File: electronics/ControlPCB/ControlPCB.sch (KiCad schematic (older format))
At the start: 29 parts, among them CON1 BARREL_JACK, P1 Opto1, P2 Opto2, P3 Opto3, P4 Opto4, P5 Opto5, P6 Opto6, P7 Tool, U1 POLOLU_A4988, U2 POLOLU_A4988, U3 POLOLU_A4988, U4 POLOLU_A4988, U5 POLOLU_A4988, U6 POLOLU_A4988, U7 POLOLU_A4988

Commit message: ControlPCB Kicad project update
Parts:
- added PA1: AUX12V, Pin_Headers:Pin_Header_Straight_2x03, symbol CONN_02X03
- added PA2: AUX5V, Pin_Headers:Pin_Header_Straight_2x03, symbol CONN_02X03
- added PDIG1: CONN_02X18, Pin_Headers:Pin_Header_Straight_2x18, symbol CONN_02X18
- added PI1: VCCINPUT, Pin_Headers:Pin_Header_Straight_1x02, symbol CONN_01X02
- added PM1, PM2, PM3, PM4, PM5, PM6, PM7: CONN_01X04, Pin_Headers:Pin_Header_Straight_1x04, symbol CONN_01X04
- C1, C2, C3, C4, C5, C6, C7: footprint (none) -> Capacitors_ThroughHole:C_Radial_D6.3_L11.2_P2.5
- CON1: value BARREL_JACK -> 12VINPUT; footprint (none) -> Connect:BARREL_JACK
- P1, P2, P3, P4, P5, P6, P7: footprint (none) -> Pin_Headers:Pin_Header_Straight_1x03
- R1, R2, R3, R4, R5, R6, R7: footprint (none) -> Resistors_ThroughHole:Resistor_Horizontal_RM7mm
- U1, U2, U3, U4, U5, U6, U7: footprint (none) -> POL:POLA4988
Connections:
- net +12V: now also PA1.2 (P2), PA1.4 (P4), PA1.6 (P6)
- net 1AM1: now also PM1.3 (P3)
- net 1AM2: now also PM2.3 (P3)
- net 1AM3: now also PM3.3 (P3)
- net 1AM4: now also PM4.3 (P3)
- net 1AM5: now also PM5.3 (P3)
- net 1AM6: now also PM6.3 (P3)
- net 1AM7: now also PM7.3 (P3)
- net 1BM1: now also PM1.4 (P4)
- net 1BM2: now also PM2.4 (P4)
- net 1BM3: now also PM3.4 (P4)
- net 1BM4: now also PM4.4 (P4)
- net 1BM5: now also PM5.4 (P4)
- net 1BM6: now also PM6.4 (P4)
- net 1BM7: now also PM7.4 (P4)
- net 2AM1: now also PM1.2 (P2)
- net 2AM2: now also PM2.2 (P2)
- net 2AM3: now also PM3.2 (P2)
- net 2AM4: now also PM4.2 (P2)
- net 2AM5: now also PM5.2 (P2)
- net 2AM6: now also PM6.2 (P2)
- net 2AM7: now also PM7.2 (P2)
- net 2BM1: now also PM1.1 (P1)
- net 2BM2: now also PM2.1 (P1)
- net 2BM3: now also PM3.1 (P1)
- net 2BM4: now also PM4.1 (P1)
- net 2BM5: now also PM5.1 (P1)
- net 2BM6: now also PM6.1 (P1)
- net 2BM7: now also PM7.1 (P1)
- net DIRM1: now also PDIG1.21 (P21)
- net DIRM2: now also PDIG1.15 (P15)
- net DIRM3: now also PDIG1.9 (P9)
- net DIRM4: now also PDIG1.3 (P3)
- net DIRM5: now also PDIG1.28 (P28)
- net DIRM6: now also PDIG1.34 (P34)
- net DIRM7: now also PDIG1.27 (P27)
- net GND: now also CON1.3, PA1.1 (P1), PA1.3 (P3), PA1.5 (P5), PA2.1 (P1), PA2.3 (P3), PA2.5 (P5), PDIG1.35 (P35), PDIG1.36 (P36), PI1.1 (P1)
- net SOPTO1: now also PDIG1.16 (P16)
- net SOPTO2: now also PDIG1.14 (P14)
- net SOPTO3: now also PDIG1.12 (P12)
- net SOPTO4: now also PDIG1.10 (P10)
- net SOPTO5: now also PDIG1.8 (P8)
- net SOPTO6: now also PDIG1.6 (P6)
- net STEPM1: now also PDIG1.23 (P23)
- net STEPM2: now also PDIG1.17 (P17)
- net STEPM3: now also PDIG1.11 (P11)
- net STEPM4: now also PDIG1.5 (P5)
- net STEPM5: now also PDIG1.26 (P26)
- net STEPM6: now also PDIG1.32 (P32)
- net STEPM7: now also PDIG1.29 (P29)
- net STOOL: now also PDIG1.4 (P4)
- net VCC: now also PA2.2 (P2), PA2.4 (P4), PA2.6 (P6), PDIG1.1 (P1), PDIG1.2 (P2), PI1.2 (P2)
- net ENABLEM1: now reaches R1.1, U1.9 (EN)
- net ENABLEM1: now also PDIG1.25 (P25)
- net ENABLEM2: now reaches R2.1, U2.9 (EN)
- net ENABLEM2: now also PDIG1.19 (P19)
- net ENABLEM3: now reaches R3.1, U3.9 (EN)
- net ENABLEM3: now also PDIG1.13 (P13)
- net ENABLEM4: now reaches R4.1, U4.9 (EN)
- net ENABLEM4: now also PDIG1.7 (P7)
- net ENABLEM5: now reaches R5.1, U5.9 (EN)
- net ENABLEM5: now also PDIG1.24 (P24)
- net ENABLEM6: now reaches R6.1, U6.9 (EN)
- net ENABLEM6: now also PDIG1.30 (P30)
- net ENABLEM7: now reaches R7.1, U7.9 (EN)
- net ENABLEM7: now also PDIG1.31 (P31)
- no-connect marks 0 -> 4
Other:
- moved on the sheet: C1, C2, C4, C5, C6, CON1, P1, P2, P3, P4, P5, P6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

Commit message: Library update
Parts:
- removed PI1: VCCINPUT, Pin_Headers:Pin_Header_Straight_1x02, symbol CONN_01X02
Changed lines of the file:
@@
 LIBS:contrib
 LIBS:valves
-LIBS:pololu_a4988
 LIBS:ControlPCB-cache
 EELAYER 25 0
@@
 	1    10050 1700
 	0    1    1    0
-$EndComp
-$Comp
-L CONN_01X02 PI1
-U 1 1 56D84F83
-P 9700 1050
-F 0 "PI1" H 9700 1200 50  0000 C CNN
-F 1 "VCCINPUT" V 9800 1050 50  0000 C CNN
-F 2 "Pin_Headers:Pin_Header_Straight_1x02" H 9700 1050 50  0001 C CNN
-F 3 "" H 9700 1050 50  0000 C CNN
-	1    9700 1050
-	1    0    0    -1
-$EndComp
-$Comp
-L GND #PWR077
-U 1 1 56D85012
-P 9400 1000
-F 0 "#PWR077" H 9400 750 50  0001 C CNN
-F 1 "GND" H 9400 850 50  0000 C CNN
-F 2 "" H 9400 1000 50  0000 C CNN
-F 3 "" H 9400 1000 50  0000 C CNN
-	1    9400 1000
-	0    1    1    0
-$EndComp
-$Comp
-L VCC #PWR078
-U 1 1 56D85074
-P 9400 1100
-F 0 "#PWR078" H 9400 950 50  0001 C CNN
-F 1 "VCC" H 9400 1250 50  0000 C CNN
-F 2 "" H 9400 1100 50  0000 C CNN
-F 3 "" H 9400 1100 50  0000 C CNN
-	1    9400 1100
-	0    -1   -1   0
 $EndComp
 Text GLabel 1600 750  0    60   Input ~ 0
@@
 	10050 1700 9950 1700
 Wire Wire Line
-	9400 1100 9500 1100
-Wire Wire Line
-	9500 1000 9400 1000
-Wire Wire Line
 	3600 2850 3600 2750

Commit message: changes added
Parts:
- removed PA1: AUX12V, Pin_Headers:Pin_Header_Straight_2x03, symbol CONN_02X03
- added C8: CP1_Small, Capacitors_ThroughHole:C_Radial_D6.3_L11.2_P2.5, symbol CP1_Small
- added D1: D_Small, symbol D_Small
- added DLED1: LEDFAN, symbol LED
- added DLED2: LED12V, symbol LED
- added DLED3: LED5V, symbol LED
- added F1: F_Small, symbol F_Small
- added P1, P2, P3, P4, P5, P6, P7, P8: CONN_02X03, symbol CONN_02X03
- added PA1: AUX12V, symbol CONN_02X10
- added PM8: CONN_01X04, Pin_Headers:Pin_Header_Straight_1x04, symbol CONN_01X04
- added PS7: Opto7, Pin_Headers:Pin_Header_Straight_1x03, symbol CONN_01X03
- added PS8: Opto8, Pin_Headers:Pin_Header_Straight_1x03, symbol CONN_01X03
- added PSW1: CONN_01X02, symbol CONN_01X02
- added R8: R, Resistors_ThroughHole:Resistor_Horizontal_RM7mm, symbol R
- added RLED1, RLED2: 560, symbol R
- added RLED3: 220, symbol R
- added U8: POLOLU_A4988, POL:POLA4988, symbol POLOLU_A4988
- renumbered P1 to PS1, P2 to PS2, P3 to PS3, P4 to PS4, P5 to PS5, P6 to PS6, P7 to PT1
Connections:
- net +12V: now also C8.1, PSW1.2 (P2), RLED2.2, U8.8 (VMOT); no longer CON1.1
- net DIRM1: now also PDIG1.11 (P11); no longer PDIG1.21 (P21)
- net DIRM2: now also PDIG1.12 (P12); no longer PDIG1.15 (P15)
- net DIRM3: now also PDIG1.13 (P13); no longer PDIG1.9 (P9)
- net DIRM4: now also PDIG1.14 (P14); no longer PDIG1.3 (P3)
- net DIRM5: now also PDIG1.15 (P15); no longer PDIG1.28 (P28)
- net DIRM6: now also PDIG1.16 (P16); no longer PDIG1.34 (P34)
- net DIRM7: now also PDIG1.17 (P17); no longer PDIG1.27 (P27)
- net GND: now also C8.2, D1.2 (A), DLED1.1 (K), DLED2.1 (K), DLED3.1 (K), PA1.1 (P1), PA1.11 (P11), PA1.13 (P13), PA1.15 (P15), PA1.17 (P17), PA1.19 (P19), PA1.3 (P3), PA1.5 (P5), PA1.7 (P7), PA1.9 (P9), PS7.1 (P1), PS8.1 (P1), U8.1 (GND), U8.7 (GND)
- net SOPTO1: now also PDIG1.23 (P23); no longer PDIG1.16 (P16)
- net SOPTO2: now also PDIG1.24 (P24); no longer PDIG1.14 (P14)
- net SOPTO3: now also PDIG1.25 (P25); no longer PDIG1.12 (P12)
- net SOPTO4: now also PDIG1.26 (P26); no longer PDIG1.10 (P10)
- net SOPTO5: now also PDIG1.27 (P27); no longer PDIG1.8 (P8)
- net SOPTO6: now also PDIG1.28 (P28); no longer PDIG1.6 (P6)
- net STEPM1: now also PDIG1.3 (P3); no longer PDIG1.23 (P23)
- net STEPM2: now also PDIG1.4 (P4); no longer PDIG1.17 (P17)
- net STEPM3: now also PDIG1.5 (P5); no longer PDIG1.11 (P11)
- net STEPM4: now also PDIG1.6 (P6); no longer PDIG1.5 (P5)
- net STEPM5: now also PDIG1.7 (P7); no longer PDIG1.26 (P26)
- net STEPM6: now also PDIG1.8 (P8); no longer PDIG1.32 (P32)
- net STEPM7: now also PDIG1.9 (P9); no longer PDIG1.29 (P29)
- net STOOL: now also PDIG1.22 (P22); no longer PDIG1.4 (P4)
- net VCC: now also P1.1 (P1), P1.3 (P3), P1.5 (P5), P2.1 (P1), P2.3 (P3), P2.5 (P5), P3.1 (P1), P3.3 (P3), P3.5 (P5), P4.1 (P1), P4.3 (P3), P4.5 (P5), P5.1 (P1), P5.3 (P3), P5.5 (P5), P6.1 (P1), P6.3 (P3), P6.5 (P5), P7.1 (P1), P7.3 (P3), P7.5 (P5), P8.1 (P1), P8.3 (P3), P8.5 (P5), PS7.2 (P2), PS8.2 (P2), R8.2, RLED3.2, U8.2 (VDD); no longer U1.10 (MS1), U1.11 (MS2), U1.12 (MS3), U2.10 (MS1), U2.11 (MS2), U2.12 (MS3), U3.10 (MS1), U3.11 (MS2), U3.12 (MS3), U4.10 (MS1), U4.11 (MS2), U4.12 (MS3), U5.10 (MS1), U5.11 (MS2), U5.12 (MS3), U6.10 (MS1), U6.11 (MS2), U6.12 (MS3), U7.10 (MS1), U7.11 (MS2), U7.12 (MS3)
- net DIRM8: now reaches PDIG1.18 (P18)
- net DIRM8: now also U8.16 (DIR)
- net ENABLEM1 renamed ENABLEM
- net ENABLEM: now also PDIG1.21 (P21), R2.1, R3.1, R4.1, R5.1, R6.1, R7.1, U2.9 (EN), U3.9 (EN), U4.9 (EN), U5.9 (EN), U6.9 (EN), U7.9 (EN), R8.1, U8.9 (EN); no longer PDIG1.25 (P25)
- removed net ENABLEM2: PDIG1.19 (P19), R2.1, U2.9 (EN)
- removed net ENABLEM3: PDIG1.13 (P13), R3.1, U3.9 (EN)
- removed net ENABLEM4: PDIG1.7 (P7), R4.1, U4.9 (EN)
- removed net ENABLEM5: PDIG1.24 (P24), R5.1, U5.9 (EN)
- removed net ENABLEM6: PDIG1.30 (P30), R6.1, U6.9 (EN)
- removed net ENABLEM7: PDIG1.31 (P31), R7.1, U7.9 (EN)
- new net: P1.2 (P2), U1.10 (MS1)
- new net: P1.4 (P4), U1.11 (MS2)
- new net: P1.6 (P6), U1.12 (MS3)
- new net: P2.2 (P2), U2.10 (MS1)
- new net: P2.4 (P4), U2.11 (MS2)
- new net: P2.6 (P6), U2.12 (MS3)
- new net: P3.2 (P2), U3.10 (MS1)
- new net: P3.4 (P4), U3.11 (MS2)
- new net: P3.6 (P6), U3.12 (MS3)
- new net: P4.2 (P2), U4.10 (MS1)
- new net: P4.4 (P4), U4.11 (MS2)
- new net: P4.6 (P6), U4.12 (MS3)
- new net: P5.2 (P2), U5.10 (MS1)
- new net: P5.4 (P4), U5.11 (MS2)
- new net: P5.6 (P6), U5.12 (MS3)
- new net: P6.2 (P2), U6.10 (MS1)
- new net: P6.4 (P4), U6.11 (MS2)
- new net: P6.6 (P6), U6.12 (MS3)
- new net: P7.2 (P2), U7.10 (MS1)
- new net: P7.4 (P4), U7.11 (MS2)
- new net: P7.6 (P6), U7.12 (MS3)
- new net: CON1.1, F1.2
- new net: P8.2 (P2), U8.10 (MS1)
- new net: P8.4 (P4), U8.11 (MS2)
- new net: P8.6 (P6), U8.12 (MS3)
- new net: U8.13 (RST), U8.14 (SLP)
- new net: DLED1.2 (A), RLED1.1
- new net: DLED2.2 (A), RLED2.1
- new net: DLED3.2 (A), RLED3.1
- new net 1AM8: PM8.3 (P3), U8.4 (1A)
- new net 1BM8: PM8.4 (P4), U8.3 (IB)
- new net 2AM8: PM8.2 (P2), U8.5 (2A)
- new net 2BM8: PM8.1 (P1), U8.6 (2B)
- new net SOPTO7: PDIG1.29 (P29), PS7.3 (P3)
- new net SOPTO8: PDIG1.30 (P30), PS8.3 (P3)
- new net STEPM8: PDIG1.10 (P10), U8.15 (STEP)
- new net VDD: D1.1 (K), F1.1, PA1.10 (P10), PA1.12 (P12), PA1.14 (P14), PA1.16 (P16), PA1.18 (P18), PA1.2 (P2), PA1.20 (P20), PA1.4 (P4), PA1.6 (P6), PA1.8 (P8), PSW1.1 (P1), RLED1.2
- no-connect marks 4 -> 6
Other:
- moved on the sheet: CON1, PA2, PDIG1, PM1, PM2, PM3, PM4, PM5, PM6, PM7, PS4, PS5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

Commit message: PCB update
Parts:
- added R10, R11, R12, R13, R14, R15, R16, R9: R, Resistors_SMD:R_1206_HandSoldering, symbol R
- C1, C2, C3, C4, C5, C6, C7, C8: footprint Capacitors_ThroughHole:C_Radial_D6.3_L11.2_P2.5 -> Capacitors_SMD:c_elec_6.3x5.7
- D1: footprint (none) -> Diodes_ThroughHole:Diode_DO-35_SOD27_Horizontal_RM10
- DLED1, DLED2, DLED3: footprint (none) -> LEDs:LED_1206
- F1: footprint (none) -> Fuse_Holders_and_Fuses:BladeFuse-CarType
- P1, P2, P3, P4, P5, P6, P7, P8: footprint (none) -> Pin_Headers:Pin_Header_Straight_2x03
- PA1: footprint (none) -> Pin_Headers:Pin_Header_Straight_2x10
- PSW1: footprint (none) -> Pin_Headers:Pin_Header_Straight_1x02
- R1, R2, R3, R4, R5, R6, R7, R8: footprint Resistors_ThroughHole:Resistor_Horizontal_RM7mm -> Resistors_SMD:R_1206_HandSoldering
- RLED1, RLED2, RLED3: footprint (none) -> Resistors_SMD:R_1206_HandSoldering
- U1, U2, U3, U4, U5, U6, U7, U8: footprint POL:POLA4988 -> Pololu:SWDIP8_.6W
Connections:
- net GND: now also R10.2, R11.2, R12.2, R13.2, R14.2, R15.2, R16.2, R9.2
- net at P1.2 (P2), U1.10 (MS1): now also R9.1
- net at P2.2 (P2), U2.10 (MS1): now also R10.1
- net at P3.2 (P2), U3.10 (MS1): now also R11.1
- net at P4.2 (P2), U4.10 (MS1): now also R12.1
- net at P5.2 (P2), U5.10 (MS1): now also R13.1
- net at P6.2 (P2), U6.10 (MS1): now also R14.1
- net at P7.2 (P2), U7.10 (MS1): now also R15.1
- net at P8.2 (P2), U8.10 (MS1): now also R16.1
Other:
- moved on the sheet: P1, P2, P3, P4, P5, P6, P7, P8

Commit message: ControlPCB before square
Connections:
- net VCC: now also P1.2 (P2), P1.4 (P4), P1.6 (P6), P2.2 (P2), P2.4 (P4), P2.6 (P6), P3.2 (P2), P3.4 (P4), P3.6 (P6), P4.2 (P2), P4.4 (P4), P4.6 (P6), P5.2 (P2), P5.4 (P4), P5.6 (P6), P6.2 (P2), P6.4 (P4), P6.6 (P6), P7.2 (P2), P7.4 (P4), P7.6 (P6), P8.2 (P2), P8.4 (P4), P8.6 (P6); no longer P1.1 (P1), P1.3 (P3), P1.5 (P5), P2.1 (P1), P2.3 (P3), P2.5 (P5), P3.1 (P1), P3.3 (P3), P3.5 (P5), P4.1 (P1), P4.3 (P3), P4.5 (P5), P5.1 (P1), P5.3 (P3), P5.5 (P5), P6.1 (P1), P6.3 (P3), P6.5 (P5), P7.1 (P1), P7.3 (P3), P7.5 (P5), P8.1 (P1), P8.3 (P3), P8.5 (P5)
- net at R9.1, U1.10 (MS1): now also P1.5 (P5); no longer P1.2 (P2)
- net at U1.11 (MS2): now also P1.3 (P3); no longer P1.4 (P4)
- net at U1.12 (MS3): now also P1.1 (P1); no longer P1.6 (P6)
- net at R10.1, U2.10 (MS1): now also P2.5 (P5); no longer P2.2 (P2)
- net at U2.11 (MS2): now also P2.3 (P3); no longer P2.4 (P4)
- net at U2.12 (MS3): now also P2.1 (P1); no longer P2.6 (P6)
- net at R11.1, U3.10 (MS1): now also P3.5 (P5); no longer P3.2 (P2)
- net at U3.11 (MS2): now also P3.3 (P3); no longer P3.4 (P4)
- net at U3.12 (MS3): now also P3.1 (P1); no longer P3.6 (P6)
- net at R12.1, U4.10 (MS1): now also P4.5 (P5); no longer P4.2 (P2)
- net at U4.11 (MS2): now also P4.3 (P3); no longer P4.4 (P4)
- net at U4.12 (MS3): now also P4.1 (P1); no longer P4.6 (P6)
- net at R13.1, U5.10 (MS1): now also P5.5 (P5); no longer P5.2 (P2)
- net at U5.11 (MS2): now also P5.3 (P3); no longer P5.4 (P4)
- net at U5.12 (MS3): now also P5.1 (P1); no longer P5.6 (P6)
- net at R14.1, U6.10 (MS1): now also P6.5 (P5); no longer P6.2 (P2)
- net at U6.11 (MS2): now also P6.3 (P3); no longer P6.4 (P4)
- net at U6.12 (MS3): now also P6.1 (P1); no longer P6.6 (P6)
- net at R15.1, U7.10 (MS1): now also P7.5 (P5); no longer P7.2 (P2)
- net at U7.11 (MS2): now also P7.3 (P3); no longer P7.4 (P4)
- net at U7.12 (MS3): now also P7.1 (P1); no longer P7.6 (P6)
- net at R16.1, U8.10 (MS1): now also P8.5 (P5); no longer P8.2 (P2)
- net at U8.11 (MS2): now also P8.3 (P3); no longer P8.4 (P4)
- net at U8.12 (MS3): now also P8.1 (P1); no longer P8.6 (P6)
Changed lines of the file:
@@
 F 3 "" H 4700 3950 50  0000 C CNN
 	1    4700 5150
-	1    0    0    -1
+	-1   0    0    1
 $EndComp
 $Comp
@@
 F 3 "" H 4700 2650 50  0000 C CNN
 	1    4700 3850
-	1    0    0    -1
+	-1   0    0    1
 $EndComp
 $Comp
@@
 F 3 "" H 4700 1400 50  0000 C CNN
 	1    4700 2600
-	1    0    0    -1
+	-1   0    0    1
 $EndComp
 $Comp
@@
 F 3 "" H 1150 1400 50  0000 C CNN
 	1    1150 2600
-	1    0    0    -1
+	-1   0    0    1
 $EndComp
 $Comp
@@
 F 3 "" H 1150 2650 50  0000 C CNN
 	1    1150 3850
-	1    0    0    -1
+	-1   0    0    1
 $EndComp
 $Comp
@@
 F 3 "" H 1150 3950 50  0000 C CNN
 	1    1150 5150
-	1    0    0    -1
+	-1   0    0    1
 $EndComp
 $Comp
@@
 F 3 "" H 1150 100 50  0000 C CNN
 	1    1150 1300
-	1    0    0    -1
+	-1   0    0    1
 $EndComp
 $Comp
@@
 F 3 "" H 4700 100 50  0000 C CNN
 	1    4700 1300
-	1    0    0    -1
+	-1   0    0    1
 $EndComp
 $Comp

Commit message: ControlPCB update
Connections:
- net DIRM1: now also PDIG1.17 (P17); no longer PDIG1.11 (P11)
- net DIRM2: now also PDIG1.15 (P15); no longer PDIG1.12 (P12)
- net DIRM4: now also PDIG1.11 (P11); no longer PDIG1.14 (P14)
- net DIRM5: now also PDIG1.12 (P12); no longer PDIG1.15 (P15)
- net DIRM6: now also PDIG1.14 (P14); no longer PDIG1.16 (P16)
- net DIRM7: now also PDIG1.16 (P16); no longer PDIG1.17 (P17)
- net GND: no longer PDIG1.35 (P35)
- net SOPTO2: now also PDIG1.25 (P25); no longer PDIG1.24 (P24)
- net SOPTO3: now also PDIG1.27 (P27); no longer PDIG1.25 (P25)
- net SOPTO4: now also PDIG1.29 (P29); no longer PDIG1.26 (P26)
- net SOPTO5: now also PDIG1.30 (P30); no longer PDIG1.27 (P27)
- net SOPTO7: now also PDIG1.26 (P26); no longer PDIG1.29 (P29)
- net SOPTO8: now also PDIG1.24 (P24); no longer PDIG1.30 (P30)
- net STEPM1: now also PDIG1.9 (P9); no longer PDIG1.3 (P3)
- net STEPM2: now also PDIG1.7 (P7); no longer PDIG1.4 (P4)
- net STEPM4: now also PDIG1.3 (P3); no longer PDIG1.6 (P6)
- net STEPM5: now also PDIG1.4 (P4); no longer PDIG1.7 (P7)
- net STEPM6: now also PDIG1.6 (P6); no longer PDIG1.8 (P8)
- net STEPM7: now also PDIG1.8 (P8); no longer PDIG1.9 (P9)
- no-connect marks 6 -> 7
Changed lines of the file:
@@
 ENABLEM
-$Comp
-L GND #PWR062
-U 1 1 56D91FA1
-P 9750 4050
-F 0 "#PWR062" H 9750 3800 50  0001 C CNN
-F 1 "GND" H 9750 3900 50  0000 C CNN
-F 2 "" H 9750 4050 50  0000 C CNN
-F 3 "" H 9750 4050 50  0000 C CNN
-	1    9750 4050
-	0    1    1    0
-$EndComp
 $Comp
 L GND #PWR063
@@
 $EndComp
 Text GLabel 9750 2450 0    60   Output ~ 0
-STEPM1
+STEPM4
 Text GLabel 9750 2850 0    60   Output ~ 0
-DIRM1
+DIRM4
 Text GLabel 9750 2550 0    60   Output ~ 0
 STEPM3
@@
 DIRM3
 Text GLabel 9750 2650 0    60   Output ~ 0
+STEPM2
+Text GLabel 9750 3050 0    60   Output ~ 0
+DIRM2
+Text GLabel 9750 2750 0    60   Output ~ 0
+STEPM1
+Text GLabel 9750 3150 0    60   Output ~ 0
+DIRM1
+Text GLabel 10450 2450 2    60   Output ~ 0
 STEPM5
-Text GLabel 9750 3050 0    60   Output ~ 0
+Text GLabel 10450 2850 2    60   Output ~ 0
 DIRM5
-Text GLabel 9750 2750 0    60   Output ~ 0
+Text GLabel 10450 2550 2    60   Output ~ 0
+STEPM6
+Text GLabel 10450 2950 2    60   Output ~ 0
+DIRM6
+Text GLabel 10450 2650 2    60   Output ~ 0
 STEPM7
-Text GLabel 9750 3150 0    60   Output ~ 0
+Text GLabel 10450 3050 2    60   Output ~ 0
 DIRM7
-Text GLabel 10450 2450 2    60   Output ~ 0
-STEPM2
-Text GLabel 10450 2850 2    60   Output ~ 0
-DIRM2
-Text GLabel 10450 2550 2    60   Output ~ 0
-STEPM4
-Text GLabel 10450 2950 2    60   Output ~ 0
-DIRM4
-Text GLabel 10450 2650 2    60   Output ~ 0
-STEPM6
-Text GLabel 10450 3050 2    60   Output ~ 0
-DIRM6
 Text GLabel 9750 3450 0    60   Input ~ 0
 SOPTO1
 Text GLabel 10450 3450 2    60   Input ~ 0
+SOPTO8
+Text GLabel 9750 3550 0    60   Input ~ 0
 SOPTO2
-Text GLabel 9750 3550 0    60   Input ~ 0
+Text GLabel 10450 3550 2    60   Input ~ 0
+SOPTO7
+Text GLabel 9750 3650 0    60   Input ~ 0
 SOPTO3
-Text GLabel 10450 3550 2    60   Input ~ 0
-SOPTO4
-Text GLabel 9750 3650 0    60   Input ~ 0
-SOPTO5
 Text GLabel 10450 3650 2    60   Input ~ 0
 SOPTO6
@@
 ENABLEM
 Text GLabel 9750 3750 0    60   Input ~ 0
-SOPTO7
+SOPTO4
 Text GLabel 10450 3750 2    60   Input ~ 0
-SOPTO8
+SOPTO5
 NoConn ~ 10350 3950
 NoConn ~ 10350 3850
@@
 Wire Wire Line
 	9850 2350 9750 2350
-Wire Wire Line
-	9750 4050 9850 4050
 Wire Wire Line
 	10450 4050 10350 4050
@@
 	4650 4850 4950 4850
 Connection ~ 4950 4950
+NoConn ~ 9850 4050
 $EndSCHEMATC

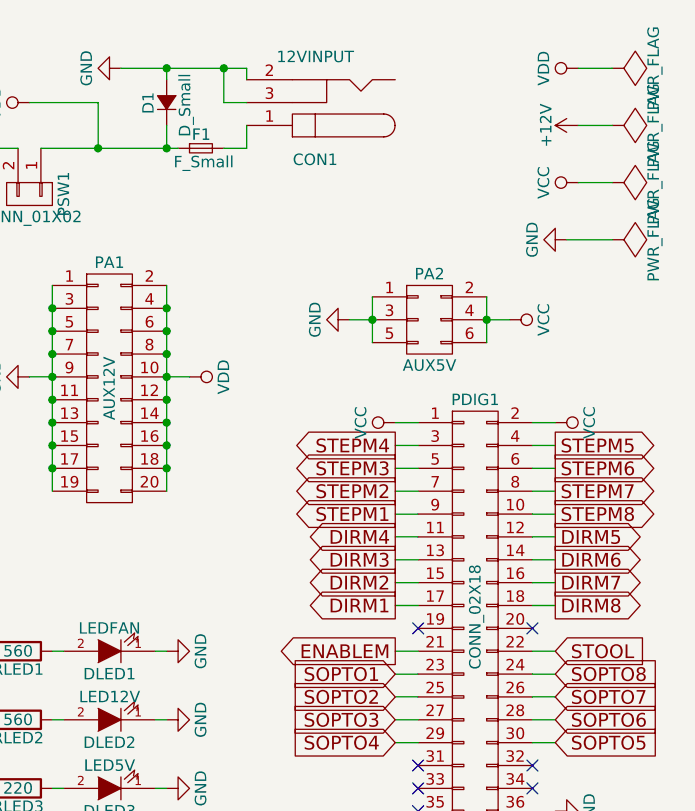
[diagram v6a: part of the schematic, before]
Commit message: ControlPCB silkscreen cleaned!
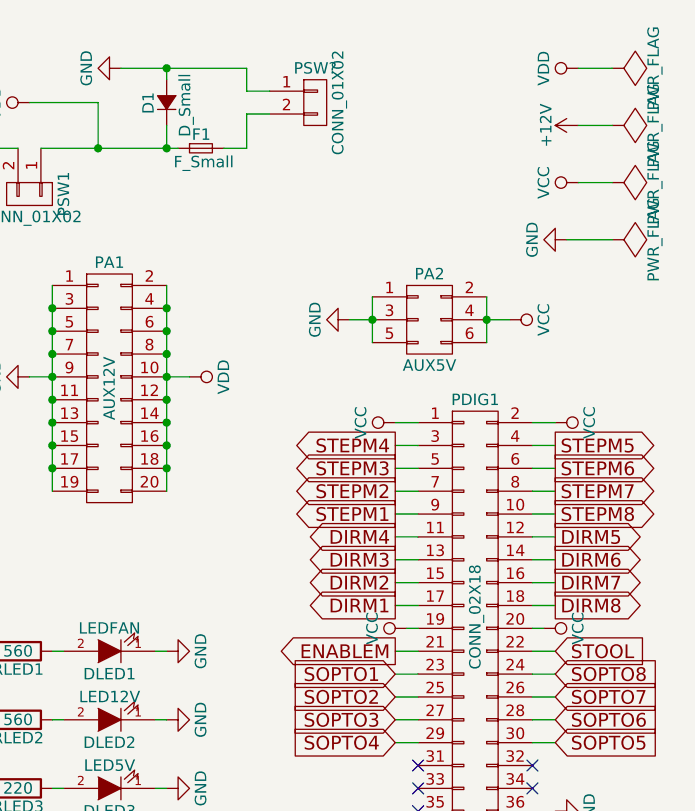
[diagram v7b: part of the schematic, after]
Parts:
- removed CON1: 12VINPUT, Connect:BARREL_JACK, symbol BARREL_JACK
- added PSW?: CONN_01X02, Pin_Headers:Pin_Header_Straight_1x02, symbol CONN_01X02
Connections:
- net GND: now also PSW?.1 (P1)
- net VCC: now also PDIG1.19 (P19), PDIG1.20 (P20)
- net at F1.2: now also PSW?.2 (P2)
- no-connect marks 7 -> 5

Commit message: Gerber files uploaded
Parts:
- gave numbers to parts that had none: 1
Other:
- moved on the sheet: F1
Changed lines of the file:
@@
 L F_Small F1
 U 1 1 58303340
-P 8900 1150
-F 0 "F1" H 8860 1210 50  0000 L CNN
-F 1 "F_Small" H 8780 1090 50  0000 L CNN
-F 2 "Fuse_Holders_and_Fuses:BladeFuse-CarType" H 8900 1150 50  0001 C CNN
-F 3 "" H 8900 1150 50  0000 C CNN
-	1    8900 1150
+P 8950 1150
+F 0 "F1" H 8910 1210 50  0000 L CNN
+F 1 "F_Small" H 8830 1090 50  0000 L CNN
+F 2 "Fuse_Holders_and_Fuses:BladeFuse-CarType" H 8950 1150 50  0001 C CNN
+F 3 "" H 8950 1150 50  0000 C CNN
+	1    8950 1150
 	1    0    0    -1
 $EndComp
@@
 	9100 1000 9100 1150
 Wire Wire Line
-	9100 1150 9000 1150
-Wire Wire Line
 	8750 1150 8750 1050
 Connection ~ 8750 1150
@@
 Connection ~ 8750 800
 Wire Wire Line
-	8200 1150 8800 1150
+	8200 1150 8850 1150
 Wire Wire Line
 	8100 1150 8000 1150
@@
 	9850 3250 9800 3250
 $Comp
-L CONN_01X02 PSW?
+L CONN_01X02 POWERPIN1
 U 1 1 58406269
 P 9400 950
-F 0 "PSW?" H 9400 1100 50  0000 C CNN
+F 0 "POWERPIN1" H 9400 1100 50  0000 C CNN
 F 1 "CONN_01X02" V 9500 950 50  0000 C CNN
 F 2 "Pin_Headers:Pin_Header_Straight_1x02" H 9400 950 50  0001 C CNN
@@
 Wire Wire Line
 	9200 1000 9100 1000
+Wire Wire Line
+	9100 1150 9050 1150
 $EndSCHEMATC
